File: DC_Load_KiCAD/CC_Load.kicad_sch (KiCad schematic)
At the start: 99 parts, among them J1 CONN_V_SENSE, J10 CONN_LED, J11 CONN_ICSP, J12 CONN_PINS, J2 CONN_FAN, J3 CONN_PWR, J4 CONN_PWR_LED, J5 USBC_CONN, J6 CONN_NTC, J7 CONN_LOAD, J8 CONN_ENCODER, J9 CONN_OLED, Q1 2N7002, Q2 IRLZ44N, Q3 IRLZ44N, Q4 IRLZ44N, Q5 IRLZ44N, Q6 IRLZ44N, SW1 RST_BTN, U1 LM7805_TO220, U2 OPA4376, U3 CH340C, U4 ATmega328P-A, U5 ADC (INA219AIDR), U6 DAC (MCP4716A0T-E/CH), U7 ADR5040BRTZ, Y1 16MHz

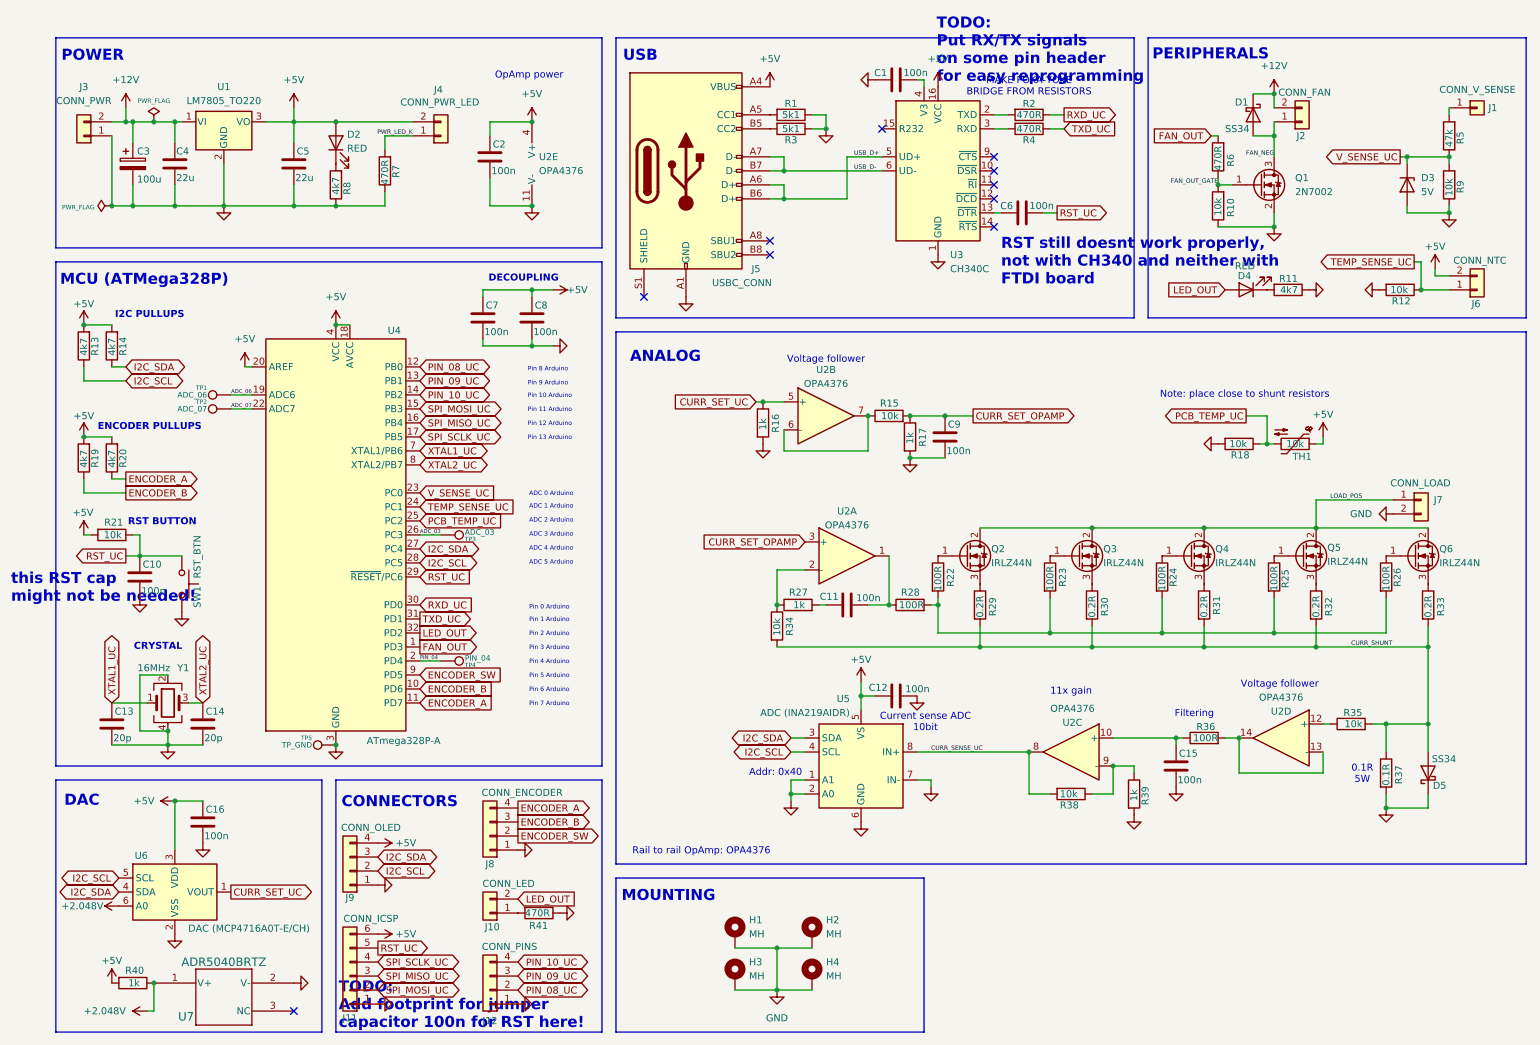
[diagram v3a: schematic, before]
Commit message: Update PCB to ver 3.0, in code updatet drivers a bit
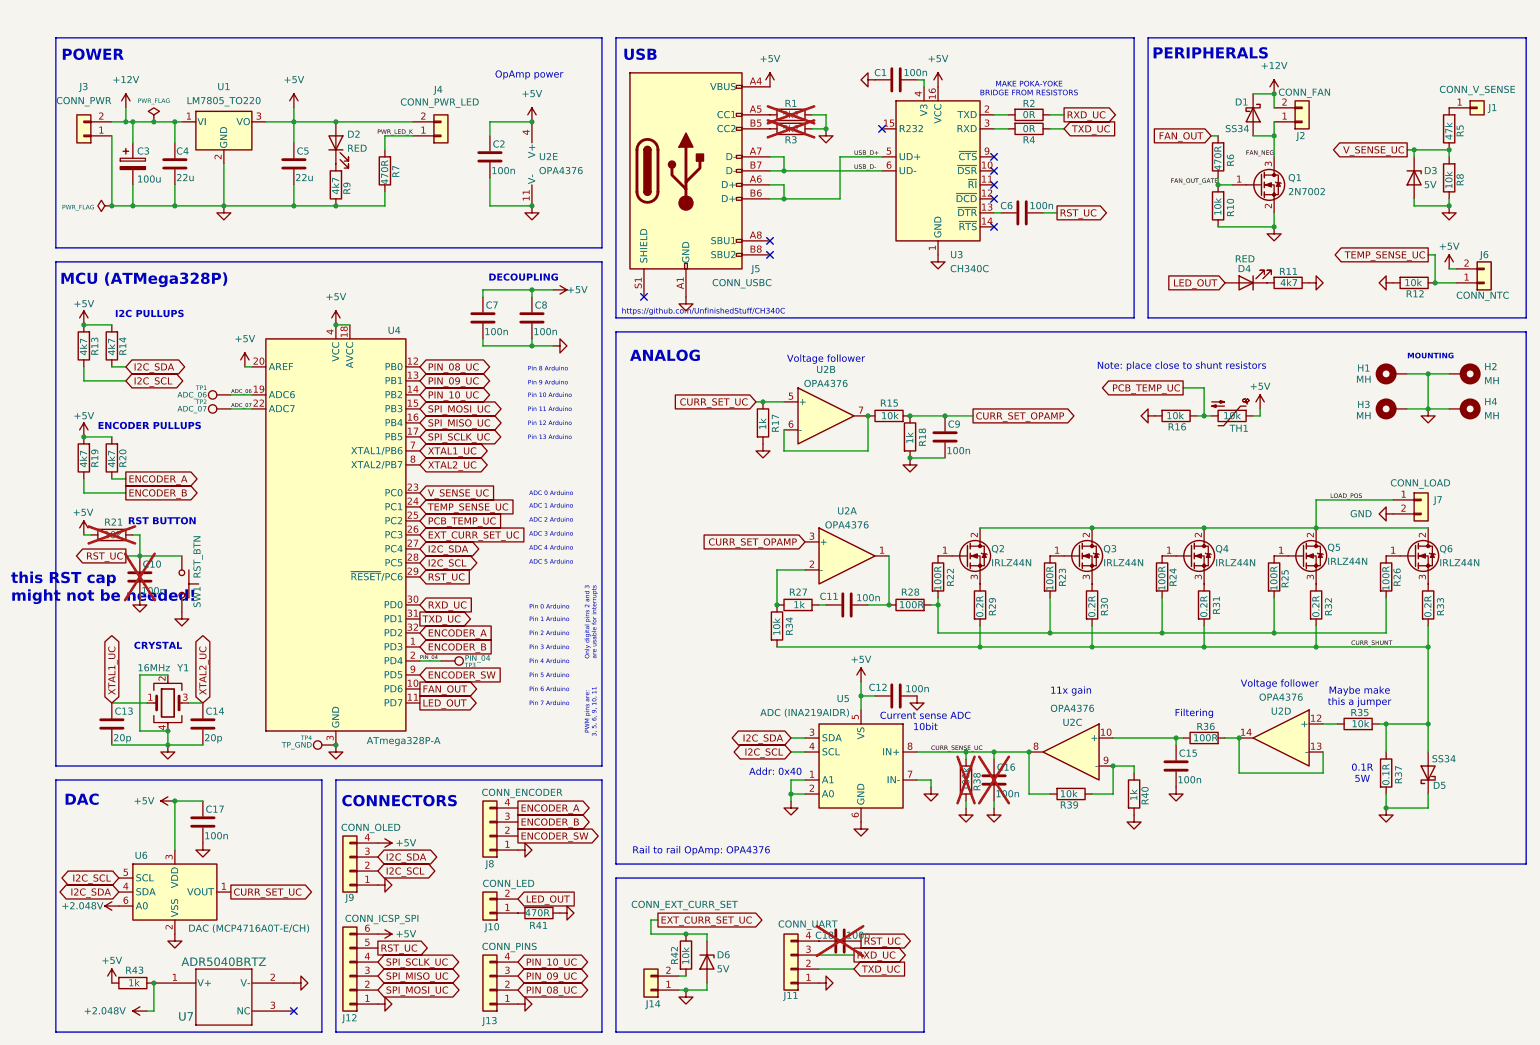
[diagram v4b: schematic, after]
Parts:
- removed TP3: ADC_03, TestPoint:TestPoint_THTPad_1.5x1.5mm_Drill0.7mm, symbol Connector:TestPoint
- added C16, C18: 100n, Capacitor_SMD:C_1206_3216Metric, symbol Device:C
- added D6: 5V, Diode_SMD:D_SOD-123, symbol Device:D_Zener
- added J11: CONN_UART, Connector_PinHeader_2.54mm:PinHeader_1x04_P2.54mm_Vertical, symbol Connector_Generic:Conn_01x04
- added J14: CONN_EXT_CURR_SET, Connector_PinHeader_2.54mm:PinHeader_1x02_P2.54mm_Vertical, symbol Connector_Generic:Conn_01x02
- added R38: 100k, Resistor_SMD:R_1206_3216Metric, symbol Device:R
- added R42: 10k, Resistor_SMD:R_1206_3216Metric, symbol Device:R
- C10, R1, R21, R3: now not fitted
- J12: renamed from J11; value CONN_ICSP -> CONN_ICSP_SPI
- J5: value USBC_CONN -> CONN_USBC
- R2, R4: value 470R -> 0R
- renumbered C16 to C17, J12 to J13, R18 to R16, R16 to R17, R17 to R18, R38 to R39, R39 to R40, R40 to R43, R9 to R8, R8 to R9, TP4 to TP3, TP5 to TP4
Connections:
- net CURR_SENSE_UC: now also C16.1, R38.1
- net ENCODER_A: now also U4.32 (PD2); no longer U4.11 (PD7)
- net ENCODER_B: now also U4.1 (PD3); no longer U4.10 (PD6)
- net FAN_OUT: now also U4.10 (PD6); no longer U4.1 (PD3)
- net GND: now also C16.2, D6.2 (A), J11.1 (Pin_1), J14.1 (Pin_1), R38.2
- net LED_OUT: now also U4.11 (PD7); no longer U4.32 (PD2)
- net RST_UC: now also C18.2
- net RXD_UC: now also J11.3 (Pin_3)
- net TXD_UC: now also J11.2 (Pin_2)
- net ADC_03 renamed EXT_CURR_SET_UC
- net EXT_CURR_SET_UC: now also D6.1 (K), R42.1
- new net: J14.2 (Pin_2), R42.2
- new net: C18.1, J11.4 (Pin_4)
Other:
- note added: "Maybe make this a jumper"
- note added: "Only digital pins 2 and 3 are usable for interrupts"
- note added: "PWM pins are: 3, 5, 6, 9, 10, 11"
- note added: "https://github.com/UnfinishedStuff/CH340C"
- note removed: "RST still doesnt work properly, not with CH340 and neither with FTDI board"
- note removed: "TODO: Add footprint for jumper capacitor 100n for RST here!"
- note removed: "TODO: Put RX/TX signals on some pin header for easy reprogramming"
- title: DC Programmable Load -> Programmable DC Load
- moved on the sheet: D3, D4, H1, H2, H3, H4, J6, R11, R12, R16, R35, R5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
